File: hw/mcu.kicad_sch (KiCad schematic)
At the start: 13 parts, among them SW1 PROV, SW2 RESET

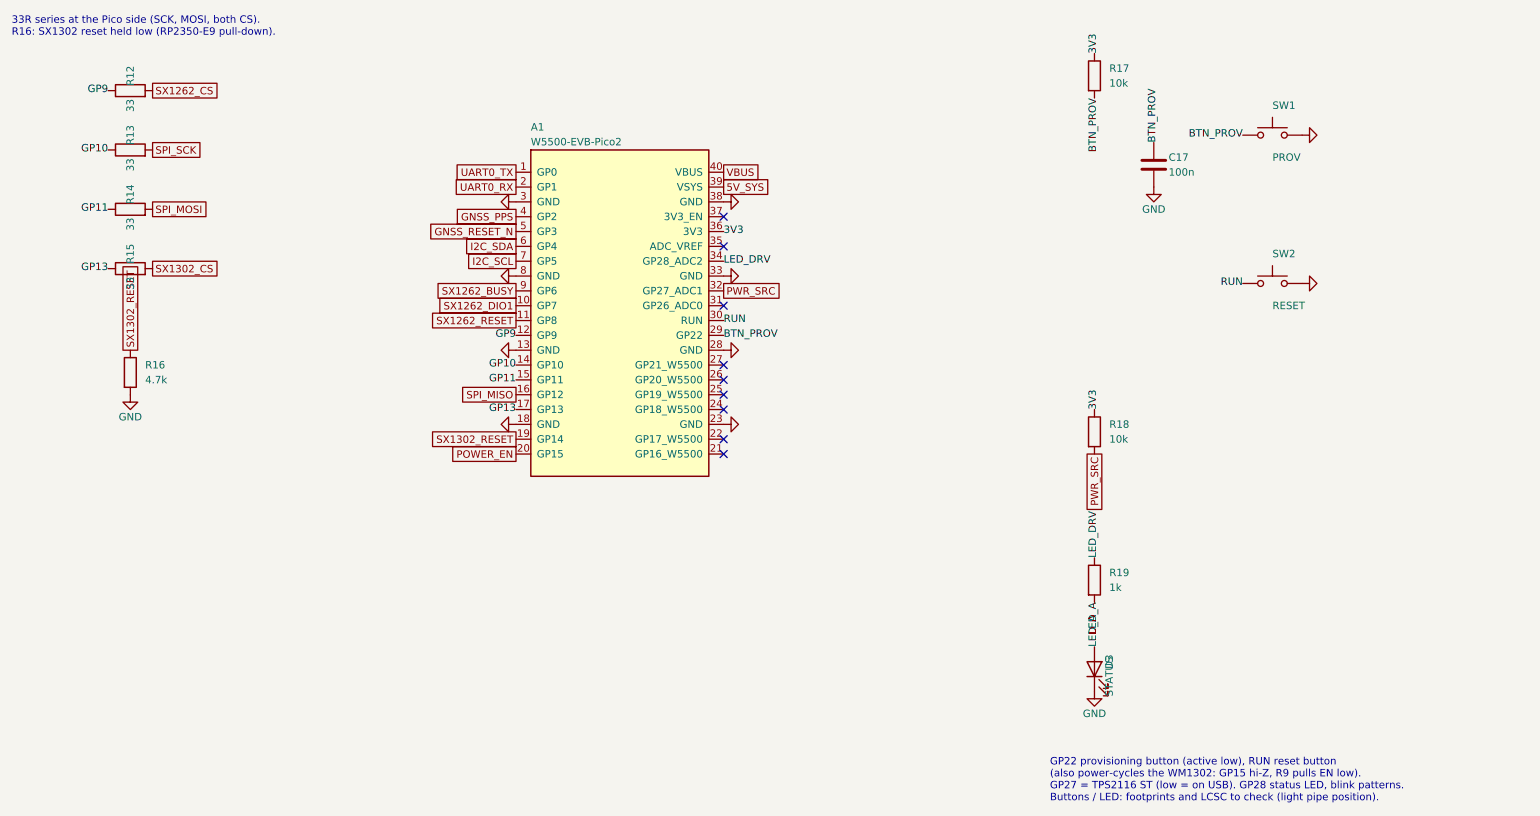
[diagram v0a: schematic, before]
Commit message: hw: draw schematic with wires instead of net labels
Connections inside a sheet are now wires; global labels remain only for
nets that cross sheets, GND stays on power symbols. Pico pins 9-20 are
fanned out so the 33R series resistors fit in one column, and the
SX1302_RESET pull-down moves to the LoRa sheet. Netlist unchanged, ERC
clean. Project file now carries KiCad's default settings.

Co-Authored-By: Claude Opus 5.5 <noreply@anthropic.com>
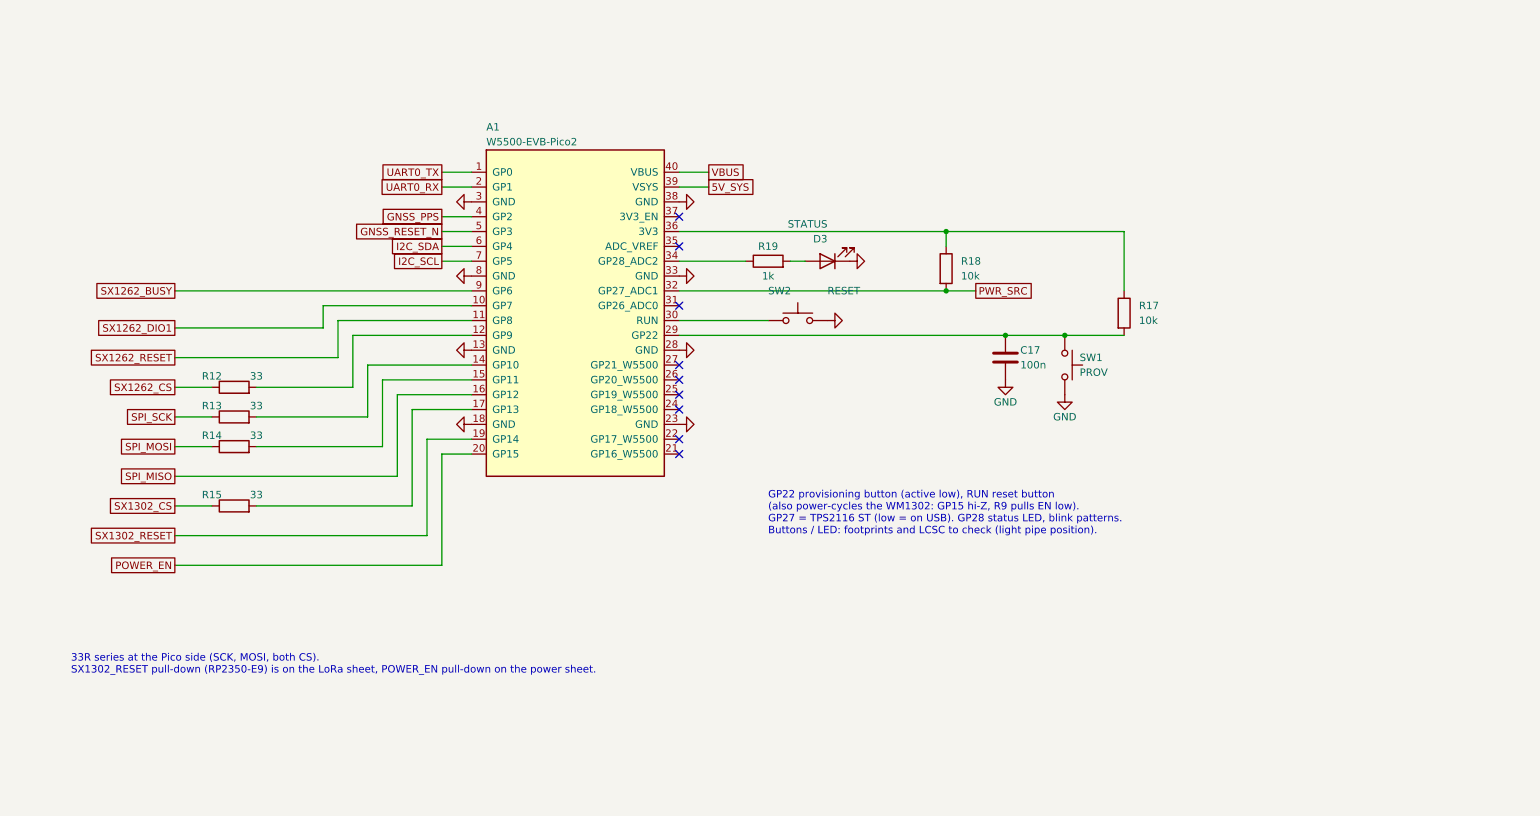
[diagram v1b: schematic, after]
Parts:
- removed R16: 4.7k, Resistor_SMD:R_0603_1608Metric, symbol Device:R
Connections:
- net SPI_MOSI: now also R14.1; no longer R14.2
- net SPI_SCK: now also R13.1; no longer R13.2
- net SX1262_CS: now also R12.1; no longer R12.2
- net SX1302_CS: now also R15.1; no longer R15.2
- net 3V3: no longer names the net of A1.36 (3V3), R17.1, R18.1
- net BTN_PROV: no longer names the net of A1.29 (GP22), C17.1, R17.2, SW1.1
- net GP10: no longer names the net of A1.14 (GP10)
- net GP10: now also R13.2; no longer R13.1
- net GP11: no longer names the net of A1.15 (GP11)
- net GP11: now also R14.2; no longer R14.1
- net GP13: no longer names the net of A1.17 (GP13)
- net GP13: now also R15.2; no longer R15.1
- net GP9: no longer names the net of A1.12 (GP9)
- net GP9: now also R12.2; no longer R12.1
- net LED_A: no longer names the net of D3.2 (A), R19.2
- net LED_DRV: no longer names the net of A1.34 (GP28_ADC2), R19.1
- net RUN: no longer names the net of A1.30 (RUN), SW2.1
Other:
- note added: "33R series at the Pico side (SCK, MOSI, both CS). SX1302_RESET pull-down (RP2350-E9) is on the LoRa sheet, POWER_EN pull-down on the power sheet."
- note removed: "33R series at the Pico side (SCK, MOSI, both CS). R16: SX1302 reset held low (RP2350-E9 pull-down)."
- moved on the sheet: A1, C17, D3, R12, R13, R14, R15, R17, R18, R19, SW1, SW2

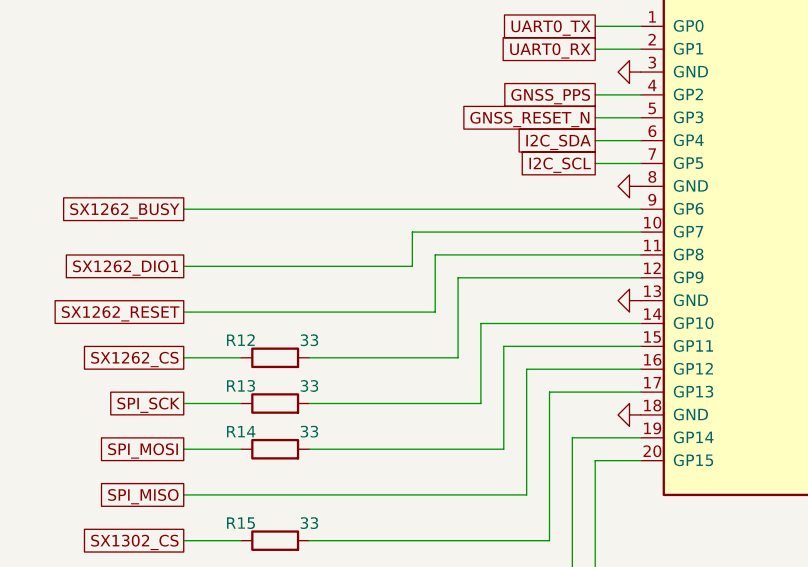
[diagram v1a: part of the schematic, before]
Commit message: sketch, hw: drop SX1262 (LBT/spectral scan), use WM1302 variant without it
LBT is not required in EU868 (ETSI duty cycle applies), so the cheaper
WM1302 SPI variant without the SX1262 is enough. Remove the SX1262 nets
and the CS series resistor R12, mark GP6-GP9 and mPCIe pins 8/10/25/33
as no-connect.

Co-Authored-By: Claude Opus 5.5 <noreply@anthropic.com>
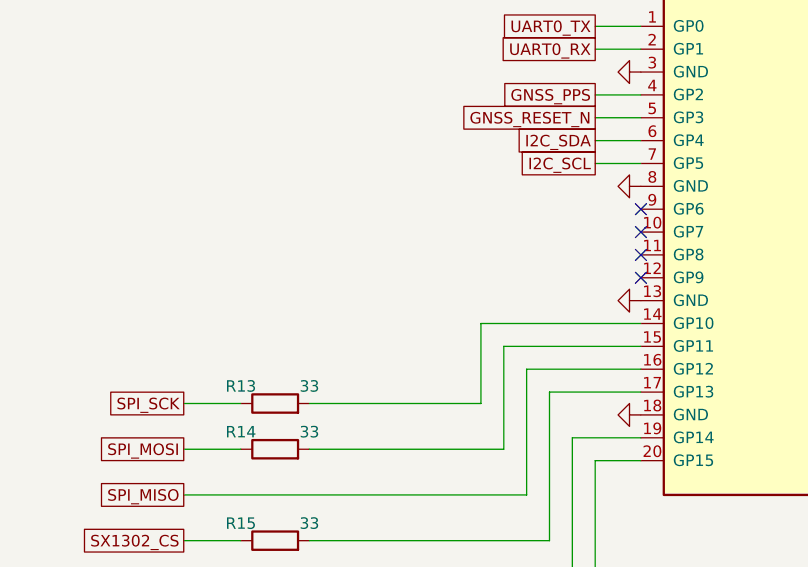
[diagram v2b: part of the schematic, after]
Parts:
- removed R12: 33, Resistor_SMD:R_0603_1608Metric, symbol Device:R
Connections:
- net SX1262_BUSY: no longer names the net of A1.9 (GP6)
- net SX1262_DIO1: no longer names the net of A1.10 (GP7)
- net SX1262_RESET: no longer names the net of A1.11 (GP8)
- no-connect marks 9 -> 13
